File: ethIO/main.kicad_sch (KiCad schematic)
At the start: 17 parts, among them J6 MISC

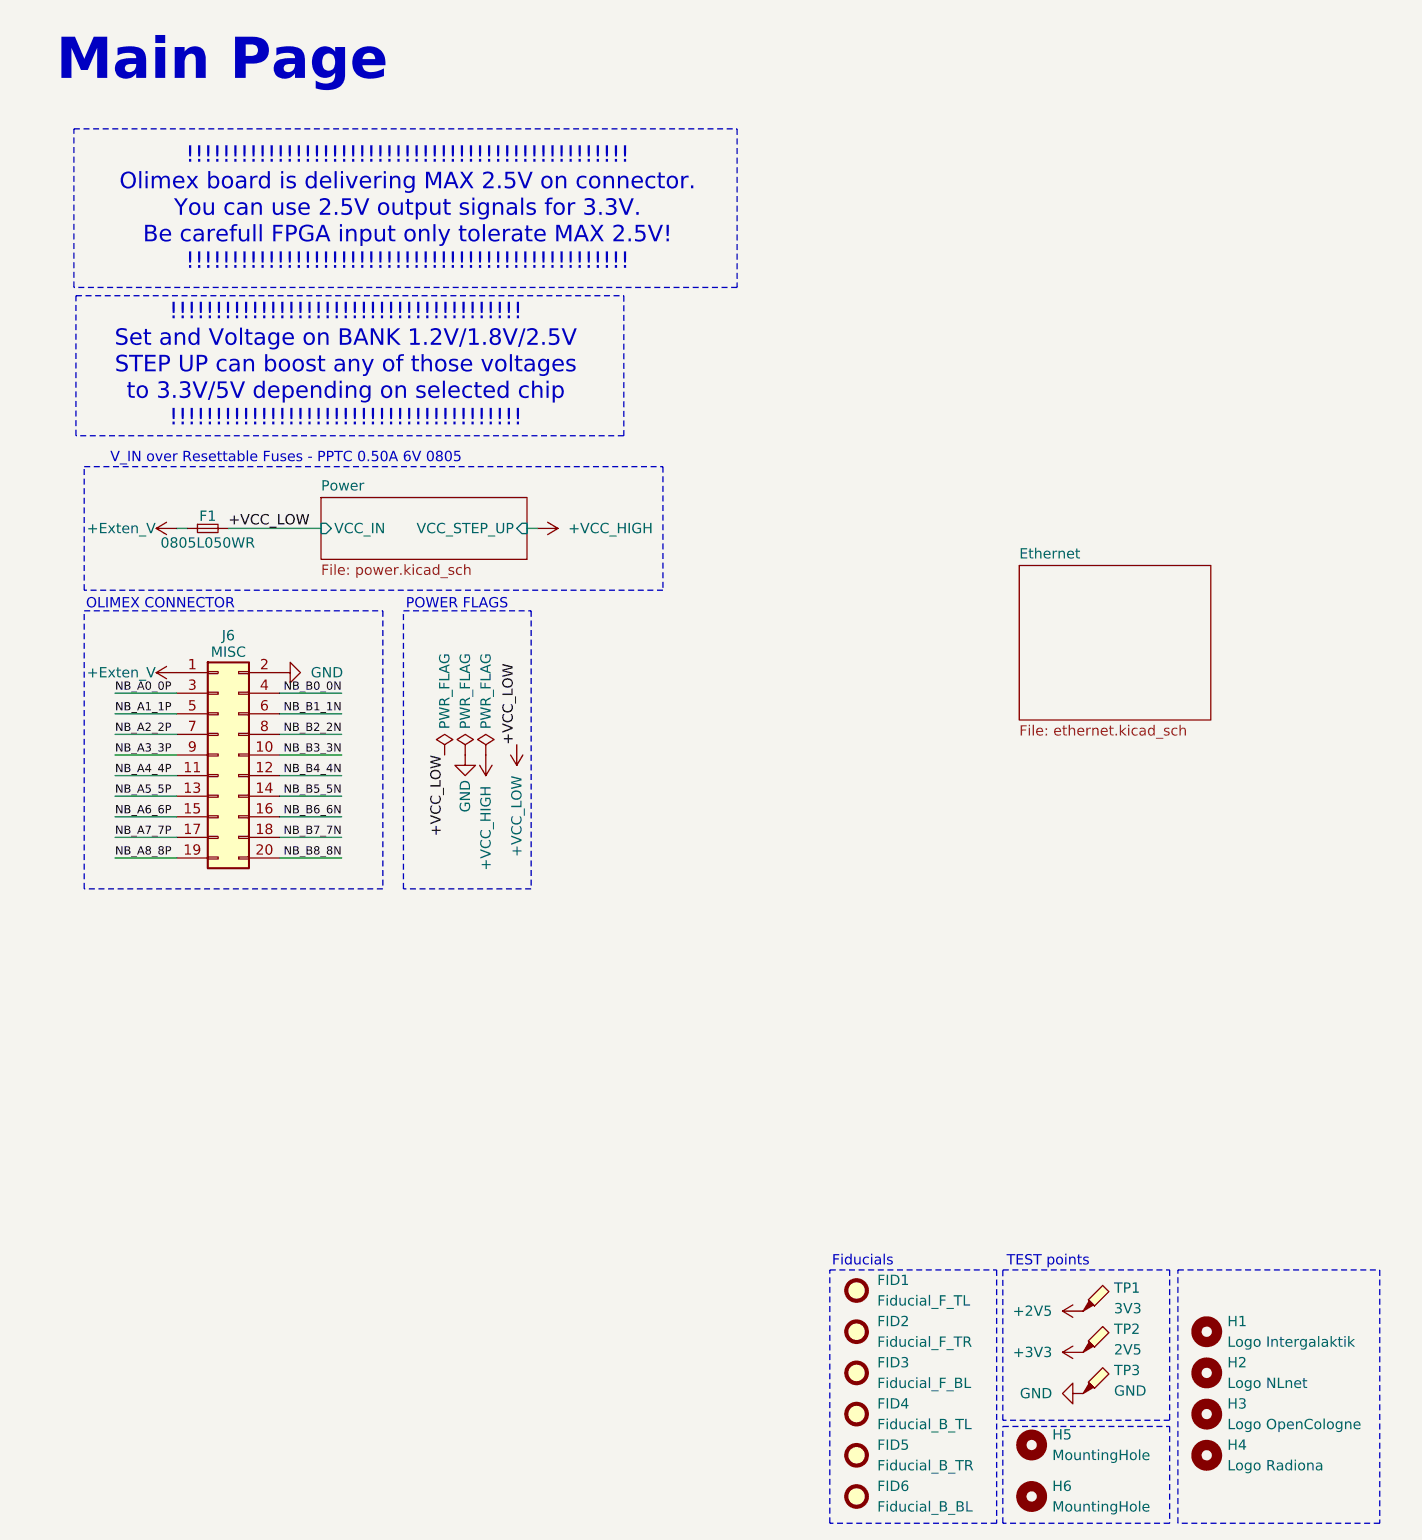
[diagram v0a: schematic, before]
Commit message: Updating ethIO
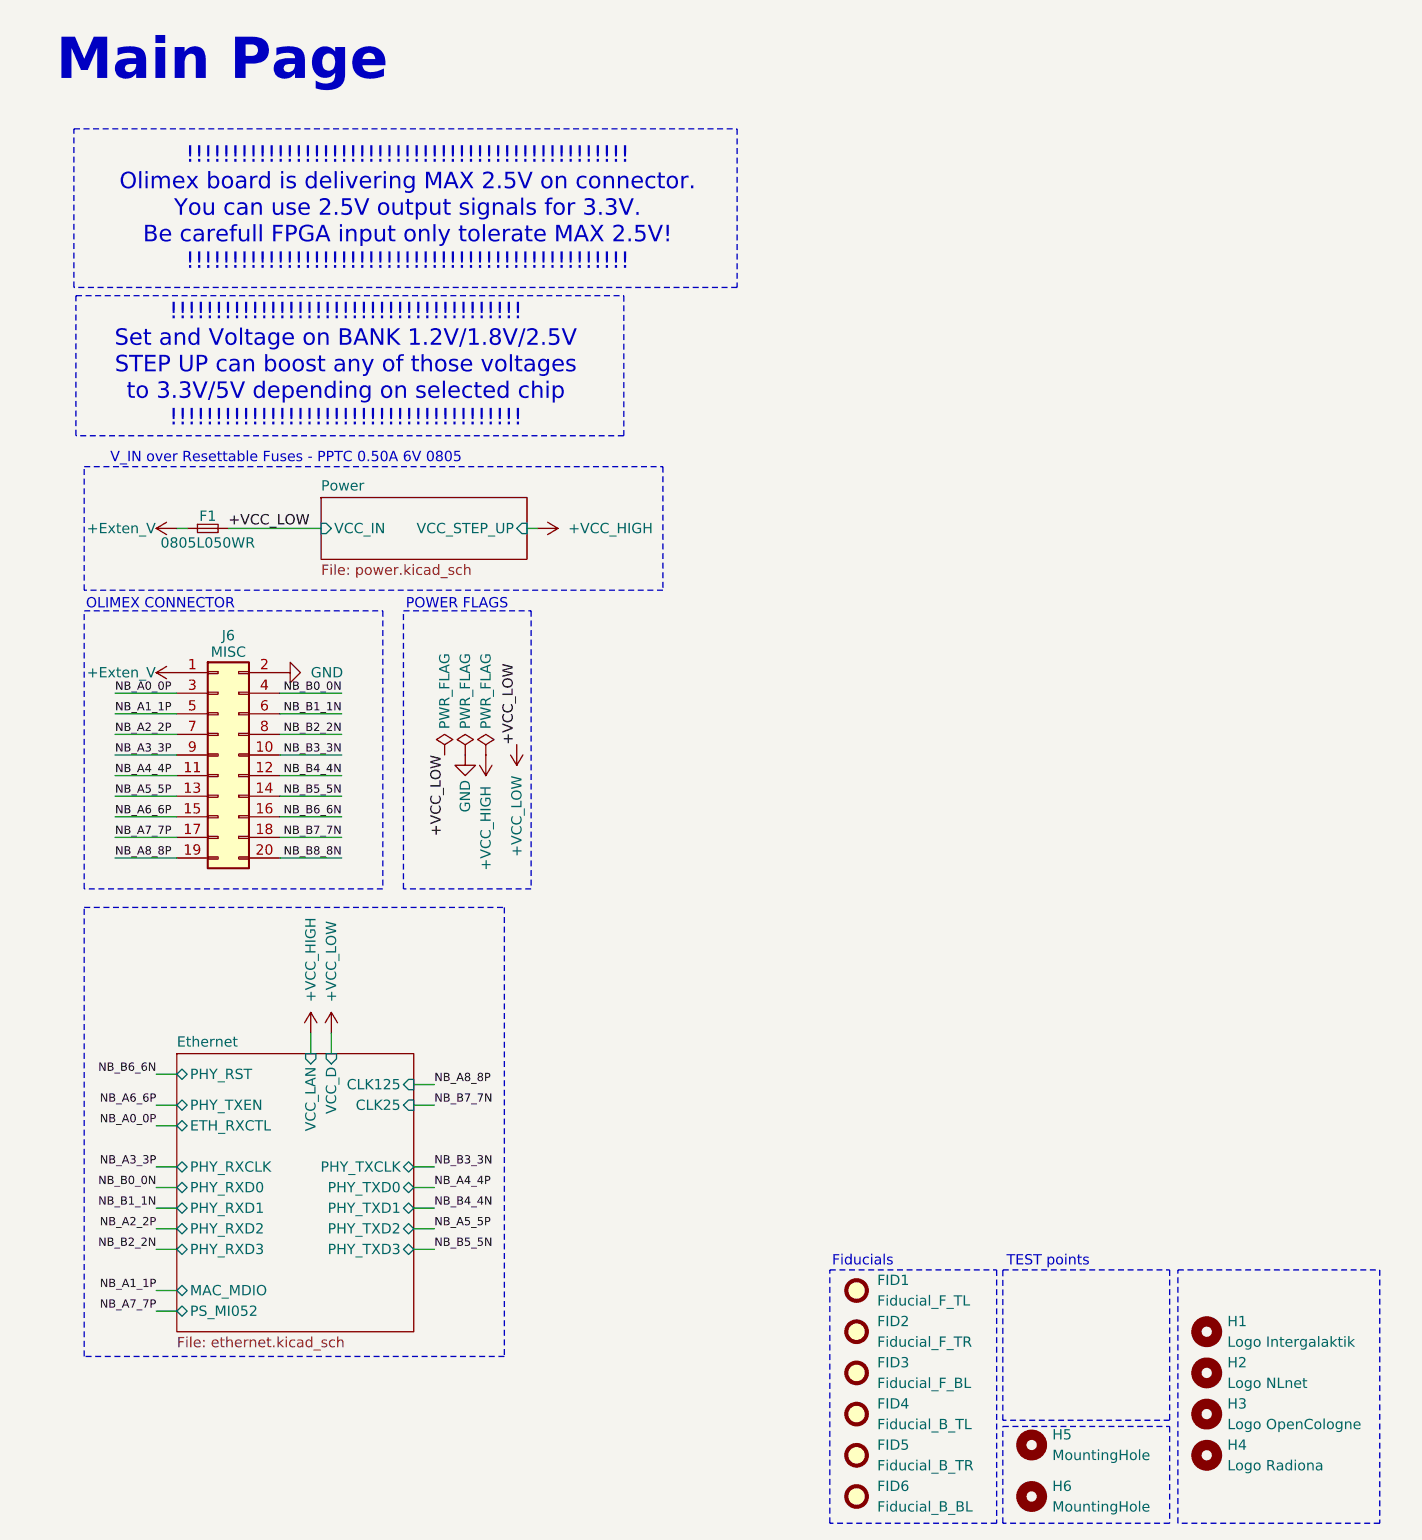
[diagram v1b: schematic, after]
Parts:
- removed TP1: 3V3, TestPoint:TestPoint_Pad_D1.0mm, symbol Connector:TestPoint_Probe
- removed TP2: 2V5, TestPoint:TestPoint_Pad_D1.0mm, symbol Connector:TestPoint_Probe
- removed TP3: GND, TestPoint:TestPoint_Pad_D1.0mm, symbol Connector:TestPoint_Probe
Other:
- sheet Ethernet ports: added CLK125, CLK25, ETH_RXCTL, MAC_MDIO, PHY_RST, PHY_RXCLK, PHY_RXD0, PHY_RXD1, PHY_RXD2, PHY_RXD3, PHY_TXCLK, PHY_TXD0, PHY_TXD1, PHY_TXD2, PHY_TXD3, PHY_TXEN, PS_MI052, VCC_D, VCC_LAN; removed none
